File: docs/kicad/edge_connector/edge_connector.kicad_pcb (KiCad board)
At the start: 2 copper layers, 119.4 x 22.9 mm, 8 parts, among them J1 Conn_01x04, J10 Conn_01x04, J2 Conn_01x04, J3 Conn_01x04, J4 Conn_01x04, J7 Conn_01x04, J8 Conn_01x04, J9 Conn_01x04

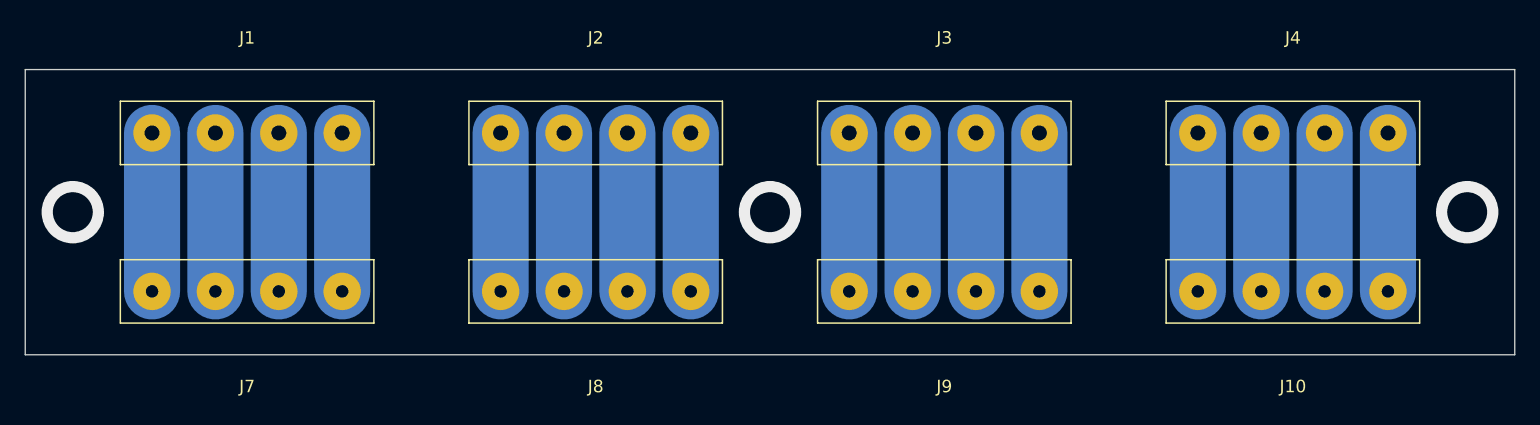
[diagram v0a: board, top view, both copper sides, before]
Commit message: change big edge connector to 5 pin (grounds for steppers)
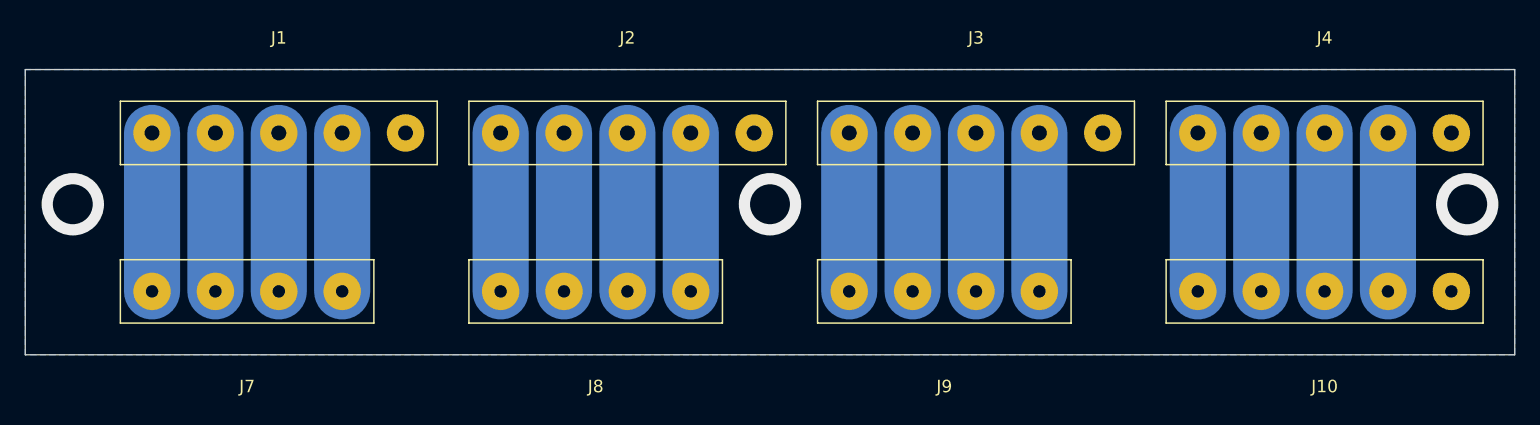
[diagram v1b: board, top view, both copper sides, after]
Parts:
- J1, J10, J2, J3, J4: value Conn_01x04 -> Conn_01x05; footprint cnc3018-PCB:big_4pin -> cnc3018-PCB:big_5pin
- moved J10 2.54 mm to (104.1, -5.08)
- moved J3 2.54 mm to (76.2, -17.8)
- moved J4 2.54 mm to (104.1, -17.8)
- moved J1 2.54 mm to (20.3, -17.8)
- moved J2 2.54 mm to (48.3, -17.8)
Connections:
- J10 pad 1: Net-(J10-Pad1) -> GND
- J4 pad 1: Net-(J10-Pad4) -> Net-(J10-Pad5)
- J4 pad 2: Net-(J10-Pad3) -> Net-(J10-Pad4)
- J4 pad 3: Net-(J10-Pad2) -> Net-(J10-Pad3)
- J4 pad 4: Net-(J10-Pad1) -> Net-(J10-Pad2)
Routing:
- net Net-(J10-Pad5): track 0.00 -> 12.7 mm
- net Net-(J10-Pad1): track 12.7 -> 0.00 mm
- net GND: vias 0 -> 3
- net (no net): vias 3 -> 0
- added copper zone on B.Cu, net GND
